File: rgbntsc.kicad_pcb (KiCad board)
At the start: 2 copper layers, 50 x 70 mm, 57 parts, among them J1 USB_C_Receptacle_Power, J2 VGA, J3 SCART_CONN, J4 Mini-DIN-4, U1 LM1881, U2 74AHCT1G86, U3 74AHCT1G86, U4 SC6206B-65K5, U5 CXA2075, U6 TPF144-VR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

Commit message: fix regulator resistor, add schematic pdf
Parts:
- R9: value 1k3 -> 1k5

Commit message: ditched supply reg, just filter harder
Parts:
- removed R8: 1k, Resistor_SMD:R_0805_2012Metric
- removed R9: 1k5, Resistor_SMD:R_0805_2012Metric
- removed U4: SC6206B-65K5, Package_TO_SOT_SMD:SOT-23
- added FB2: Ferrite_Bead_Small, Capacitor_SMD:C_0805_2012Metric, F.Cu at (47.0, 45.1)
- moved C10 6.47 mm to (47.0, 48.6), turned to 270 degrees
- moved C9 5.80 mm to (41.2, 46.9), turned to 270 degrees
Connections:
- C9 pad 1: VCC -> +5V
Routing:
- net +5V: track 5.87 -> 14.4 mm
- net VCC: track 116.7 -> 111.6 mm
- net Net-(R8-Pad2): track 4.22 -> 0.00 mm
- net GND: track 1.84 -> 1.94 mm, vias 153 -> 161

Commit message: swapping parts
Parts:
- removed U6: TPF144-VR, Package_SO:MSOP-10_3x3mm_P0.5mm
- added U4: THS7374, Package_SO:TSSOP-14_4.4x5mm_P0.65mm, F.Cu at (44.3, 98.2)
- X1: value O32253579545MHEA4SI -> S7D3.579545A20F30T; footprint Oscillator:Oscillator_SMD_Abracon_ASE-4Pin_3.2x2.5mm -> Oscillator:Oscillator_SMD_Abracon_ASV-4Pin_7.0x5.1mm
- moved GOTE1 19.3 mm to (35.2, 105.4)
- moved C11 2.06 mm to (48.1, 98.1)
- moved X1 1.88 mm to (55.5, 94.0)
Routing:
- net GND: track 1.94 -> 8.72 mm, vias 161 -> 150
- net VCC: track 111.6 -> 114.4 mm
- net Net-(C5-Pad1): track 26.7 -> 28.2 mm
- net Net-(J3-Pad2): track 43.8 -> 45.0 mm
- net Net-(C6-Pad1): track 26.9 -> 28.0 mm
- net Net-(C7-Pad1): track 21.4 -> 22.3 mm
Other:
- board text added: "RGB to NTSC 2021-05-05 rev 3.3 wakabavideo.com"
- board text removed: "RGB to NTSC 2021-06-10 rev 3.2 wakabavideo.com"

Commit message: updated gerbs, kicad 6 migration
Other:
- net class Default removed

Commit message: resync git i forgor what changed
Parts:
- X1: value S7D3.579545A20F30T -> S5D3.579545A20F30T; footprint Oscillator:Oscillator_SMD_Abracon_ASV-4Pin_7.0x5.1mm -> Oscillator:Oscillator_SMD_EuroQuartz_XO53-4Pin_5.0x3.2mm
- moved X1 0.39 mm to (55.9, 94.0)
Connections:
- J2 pad 11: Net-(J2-Pad11) -> unconnected-(J2-ID0/RES-Pad11)
- J2 pad 12: Net-(J2-Pad12) -> unconnected-(J2-ID1/SDA-Pad12)
- J2 pad 15: Net-(J2-Pad15) -> unconnected-(J2-ID3/SCL-Pad15)
- J2 pad 4: Net-(J2-Pad4) -> unconnected-(J2-ID2/RES-Pad4)
- J2 pad 9: Net-(J2-Pad9) -> unconnected-(J2-KEY/PWR-Pad9)
- J3 pad 1: Net-(J3-Pad1) -> unconnected-(J3-AUD_OUT_R-Pad1)
- J3 pad 10: Net-(J3-Pad10) -> unconnected-(J3-IOCTRL-Pad10)
- J3 pad 12: Net-(J3-Pad12) -> unconnected-(J3-RSV-Pad12)
- J3 pad 16: Net-(J3-Pad16) -> unconnected-(J3-RGB_STAT-Pad16)
- J3 pad 19: Net-(J3-Pad19) -> unconnected-(J3-SYNC_OUT-Pad19)
- J3 pad 3: Net-(J3-Pad3) -> unconnected-(J3-AUD_OUT_L-Pad3)
- U1 pad 3: Net-(U1-Pad3) -> unconnected-(U1-FRAME-Pad3)
- U1 pad 5: Net-(U1-Pad5) -> unconnected-(U1-BURST-Pad5)
- U1 pad 7: Net-(U1-Pad7) -> unconnected-(U1-O/E-Pad7)
- U4 pad 1: Net-(U4-Pad1) -> unconnected-(U4-In1-Pad1)
- U4 pad 14: Net-(U4-Pad14) -> unconnected-(U4-Out1-Pad14)
- U4 pad 7: Net-(U4-Pad7) -> unconnected-(U4-N/C-Pad7)
- U4 pad 8: Net-(U4-Pad8) -> unconnected-(U4-N/C-Pad8)
- U5 pad 21: Net-(U5-Pad21) -> unconnected-(U5-Bout-Pad21)
- U5 pad 22: Net-(U5-Pad22) -> unconnected-(U5-Gout-Pad22)
- U5 pad 23: Net-(U5-Pad23) -> unconnected-(U5-Rout-Pad23)
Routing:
- net VCC: track 114.4 -> 112.4 mm

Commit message: prod file updates
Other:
- board text added: "RGB to NTSC 2025-01-20 rev 3.4 wakabavideo.com"
- board text removed: "RGB to NTSC 2021-05-05 rev 3.3 wakabavideo.com"

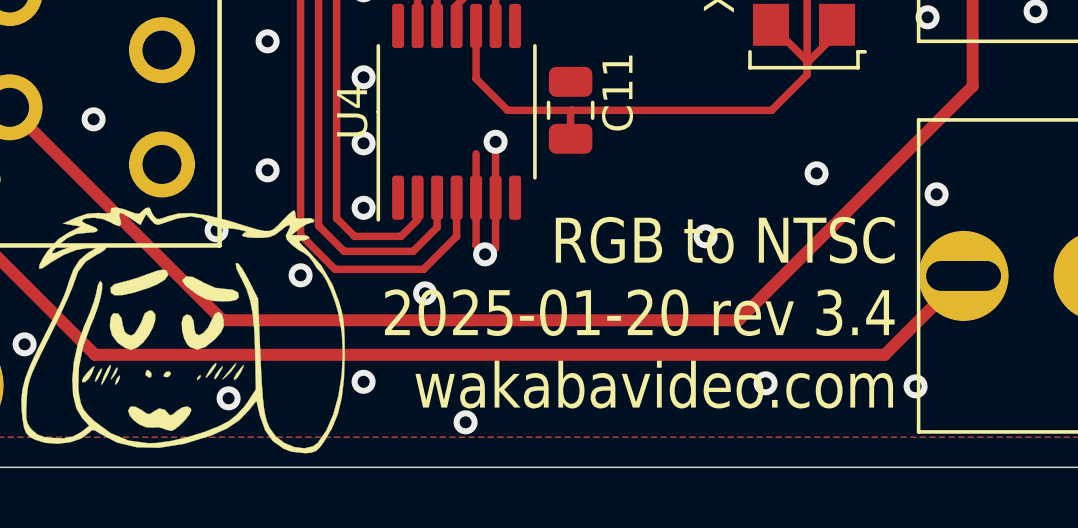
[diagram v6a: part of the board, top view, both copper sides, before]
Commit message: cover prod files
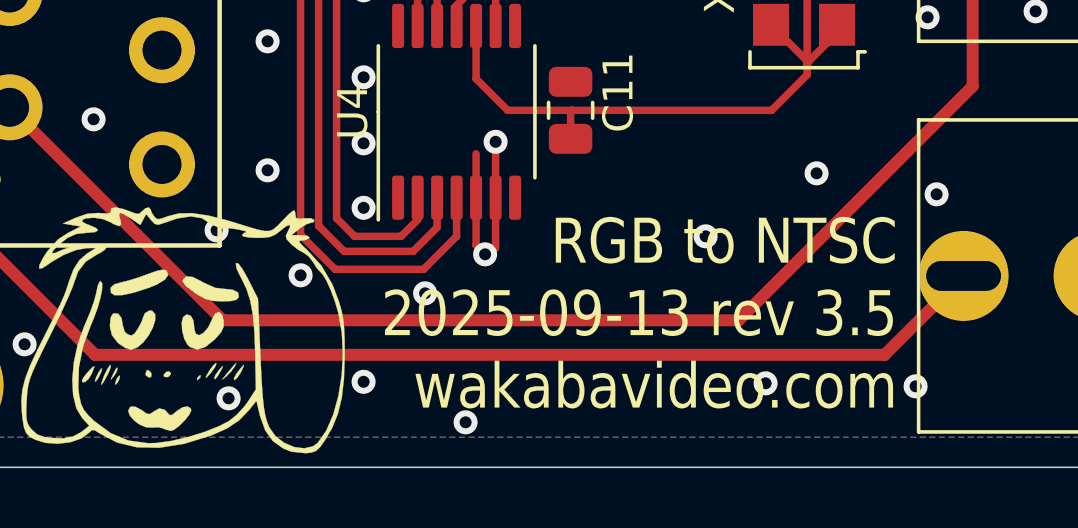
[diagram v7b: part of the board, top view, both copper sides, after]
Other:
- board text added: "RGB to NTSC 2025-09-13 rev 3.5 wakabavideo.com"
- board text removed: "RGB to NTSC 2025-01-20 rev 3.4 wakabavideo.com"
